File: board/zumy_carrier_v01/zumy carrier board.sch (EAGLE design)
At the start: 20 parts, among them IC1 SN74AUP2G17, IC2 SN74AUP2G17, J1 ODROID_POWER, J2 BATT_POWER, M1 POLOLU_STEP_DOWN, M2 ITG/MPU_MODULE, M3 POLOLU_DRV8833_MODULE, SW1 500SSP1S1M6QEA

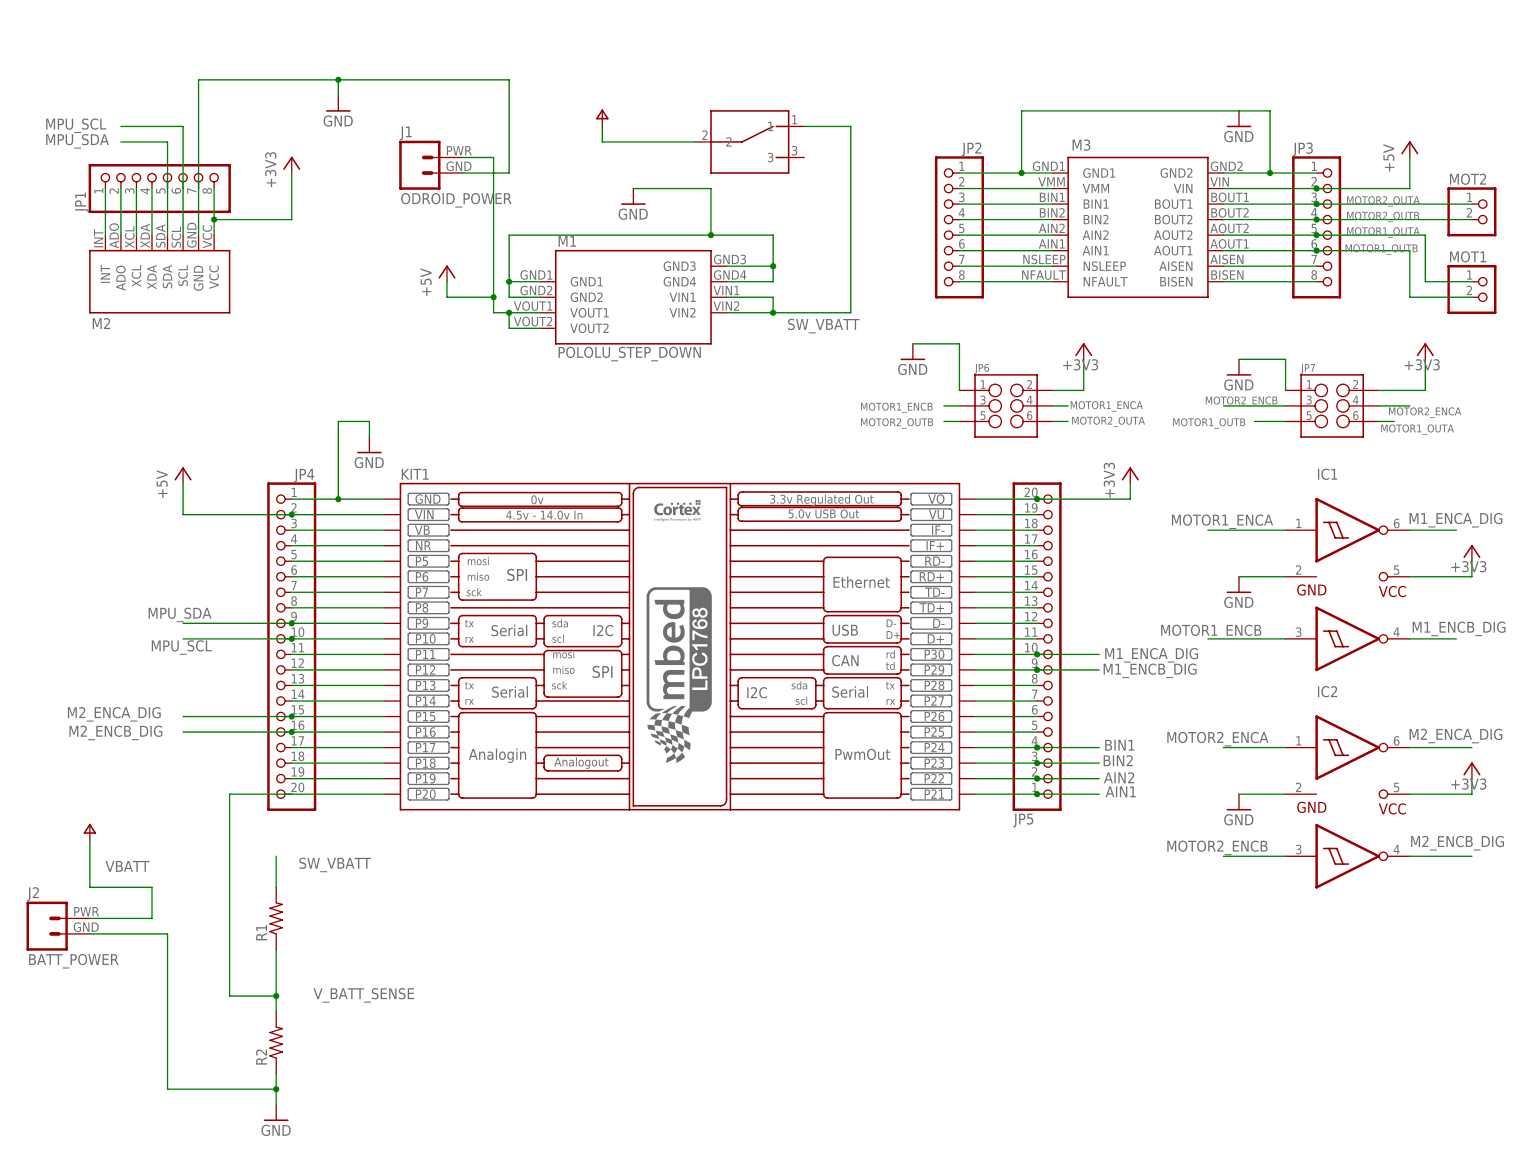
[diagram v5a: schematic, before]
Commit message: Added Rev. E Parts (5V Reg with UVLO, Cap on vsense, caps on level translators). Before ripup and rearrange.
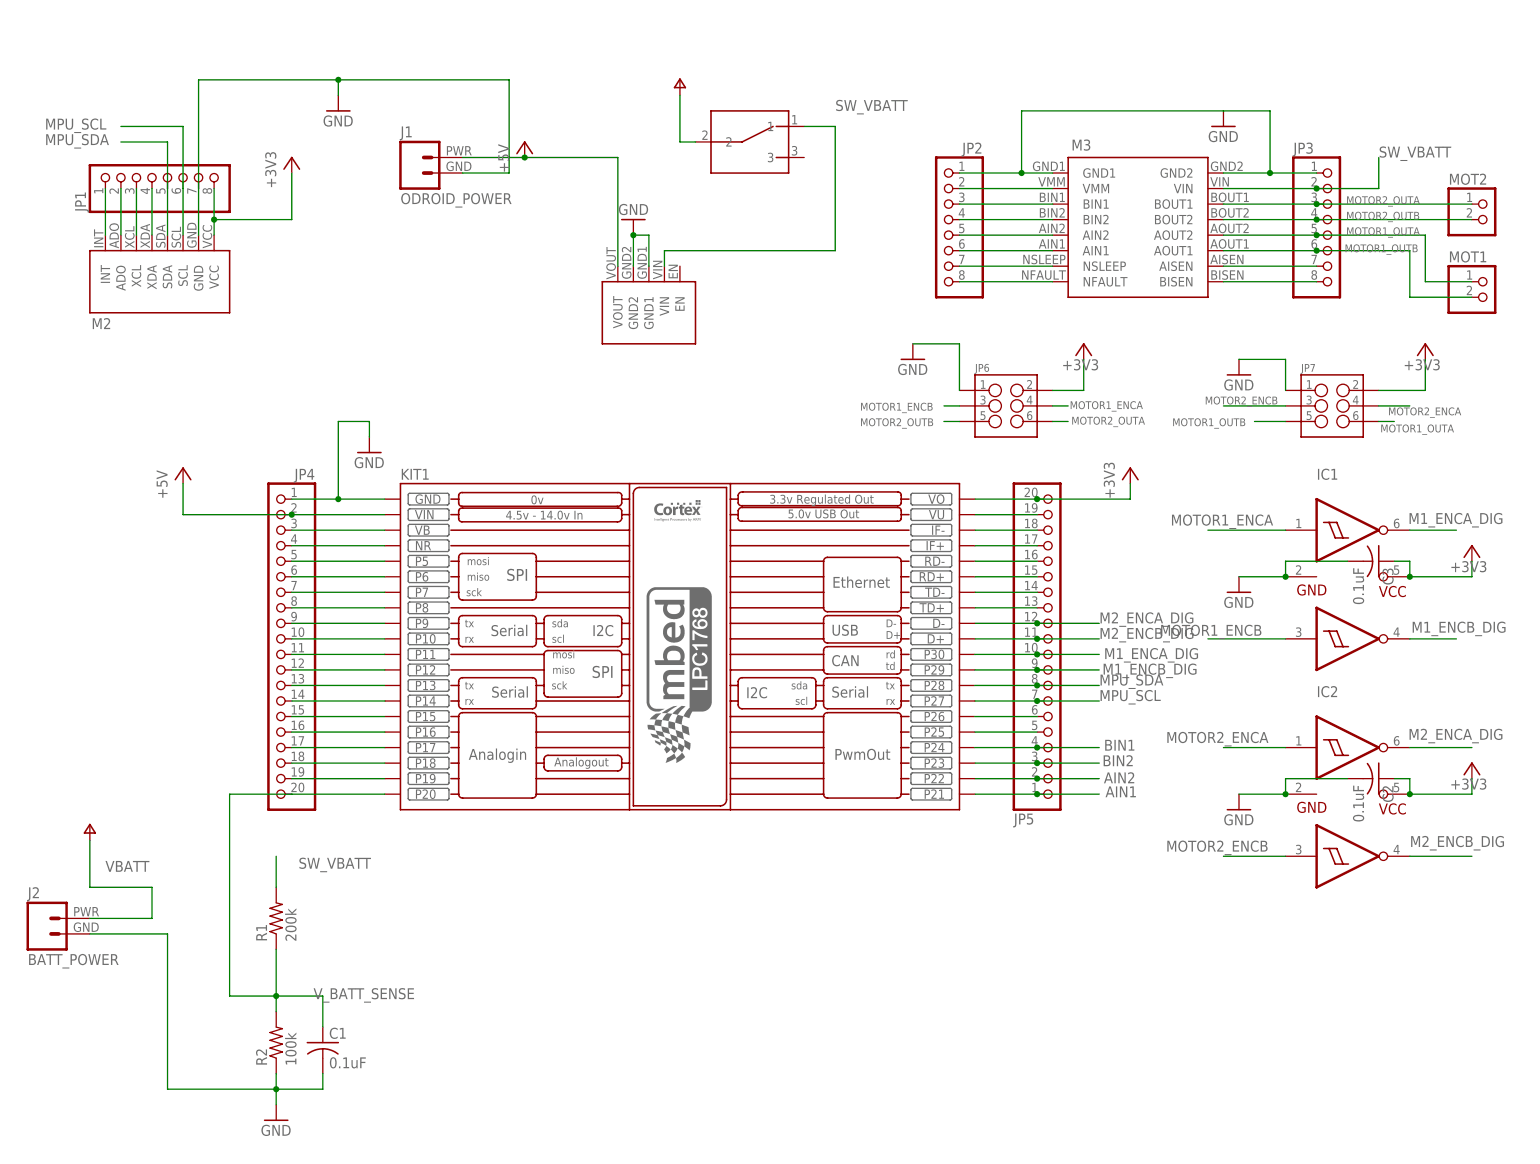
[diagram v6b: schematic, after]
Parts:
- removed M1: POLOLU_STEP_DOWN, zumy:POLOLU_STEP_DOWN
- added C1, C2, C3: 0.1uF, rcl:C-USC1206
- added U$5: POLOLU_D24V50F5, zumy:POLOLU_D24V50F5
- R1: value (none) -> 200k; device resistor:R-US_0204/5 -> resistor:R-US_R1206
- R2: value (none) -> 100k; device resistor:R-US_0204/5 -> resistor:R-US_R1206
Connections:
- removed net N$35: JP5.7, KIT1.P27
- removed net N$36: JP5.8, KIT1.P28
- removed net N$39: JP5.11, KIT1.D+
- removed net N$40: JP5.12, KIT1.D-
- new net N$10: JP4.16, KIT1.P16
- new net N$7: JP4.9, KIT1.P9
- new net N$8: JP4.10, KIT1.P10
- new net N$9: JP4.15, KIT1.P15
- net +3V3: now also C2.1, C3.1
- net +5V: now also U$5.VOUT; no longer JP3.2, M1.VOUT1, M1.VOUT2, M3.VIN
- net GND: now also C1.2, C2.2, C3.2, U$5.GND1, U$5.GND2; no longer M1.GND1, M1.GND2, M1.GND3, M1.GND4
- net M2_ENCA_DIG: now also JP5.12, KIT1.D-; no longer JP4.15, KIT1.P15
- net M2_ENCB_DIG: now also JP5.11, KIT1.D+; no longer JP4.16, KIT1.P16
- net MPU_SCL: now also JP5.7, KIT1.P27; no longer JP4.10, KIT1.P10
- net MPU_SDA: now also JP5.8, KIT1.P28; no longer JP4.9, KIT1.P9
- net SW_VBATT: now also JP3.2, M3.VIN, U$5.VIN; no longer M1.VIN1, M1.VIN2
- net V_BATT_SENSE: now also C1.1

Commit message: Schematic and part placement mostly done. Need to clean up schematic, then fine adjust layout, then ready for routing.
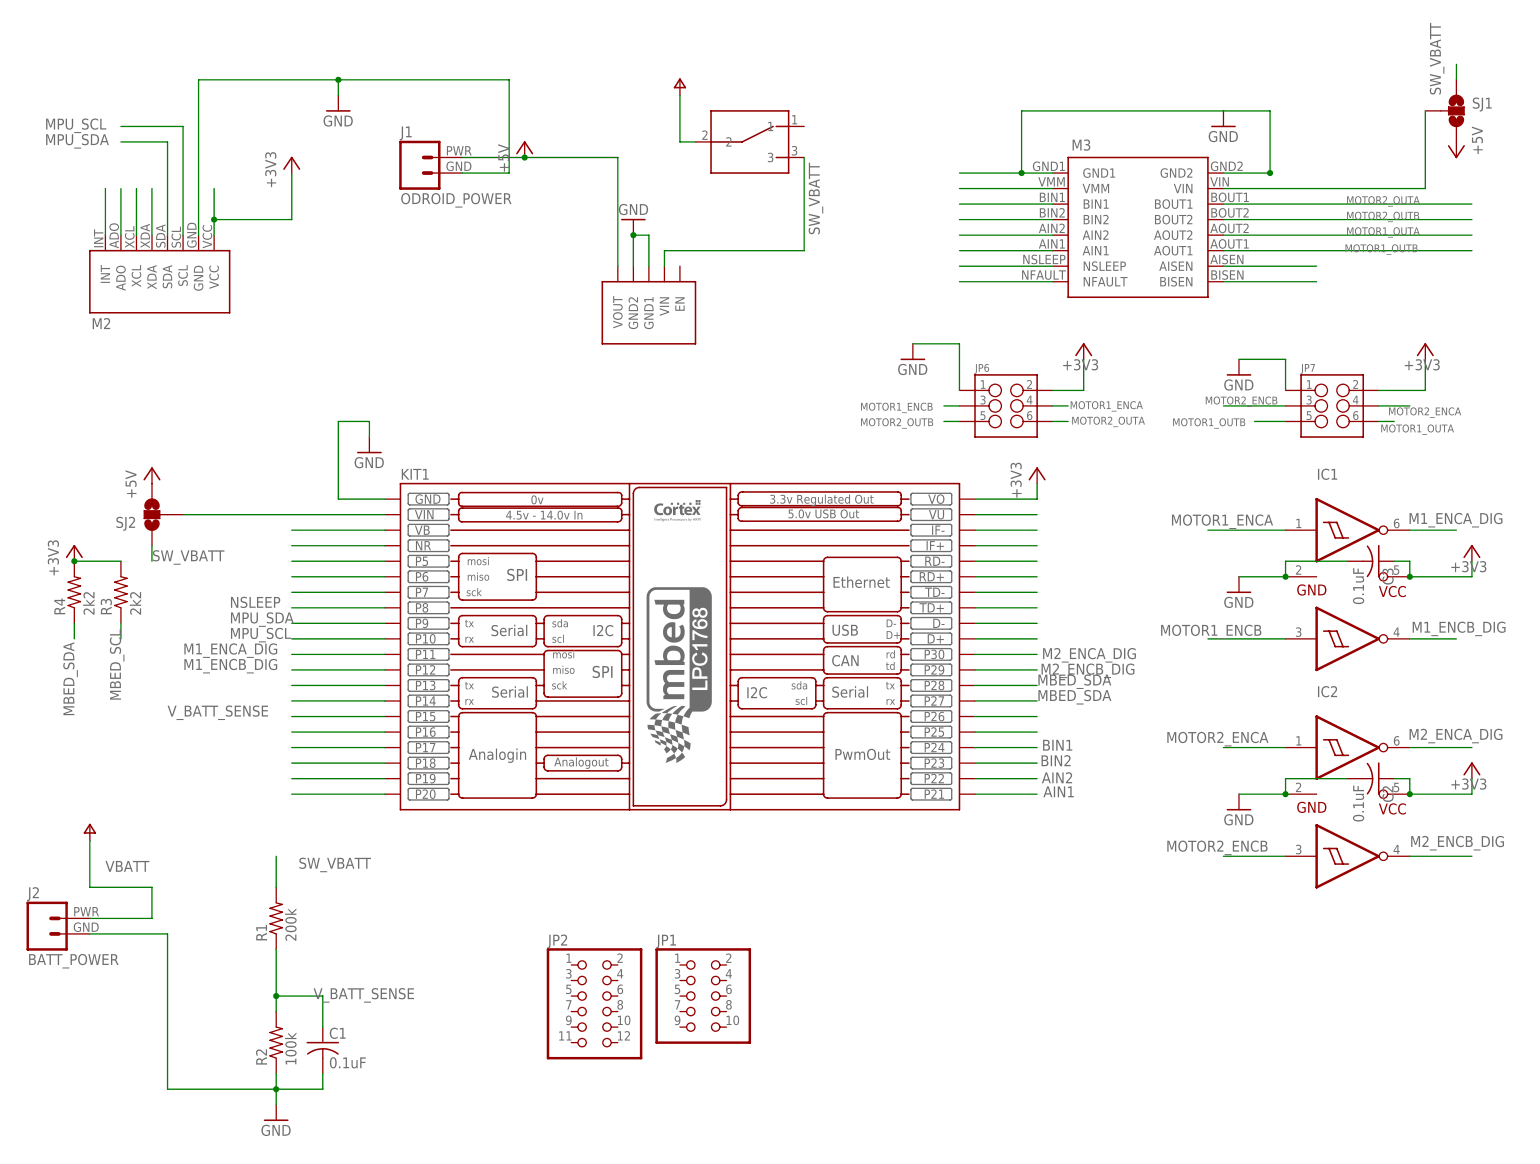
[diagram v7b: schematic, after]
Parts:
- removed JP3: (no value), zumy:PINHD-1X8
- removed JP4, JP5: (no value), zumy:PINHD-1X20
- removed MOT1, MOT2: (no value), pinhead:PINHD-1X2
- added R3, R4: 2k2, resistor:R-US_R1206
- added SJ1, SJ2: (no value), SparkFun-Passives:SOLDERJUMPER_2WAYT
- JP1: device zumy:PINHD-1X8 -> pinhead:PINHD-2X5
- JP2: device zumy:PINHD-1X8 -> pinhead:PINHD-2X6
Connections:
- removed net N$19: JP4.11, KIT1.P11
- removed net N$20: JP4.12, KIT1.P12
- removed net N$55: JP2.7, M3.NSLEEP
- removed net N$8: JP4.10, KIT1.P10
- removed net N$9: JP4.15, KIT1.P15
- new net MBED_SCL: KIT1.P27, R3.1
- new net MBED_SDA: KIT1.P28, R4.1
- new net N$17: KIT1.VIN, SJ2.2
- new net N$5: KIT1.D-
- new net N$6: KIT1.D+
- new net NSLEEP: KIT1.P8, M3.NSLEEP
- net +3V3: now also R3.2, R4.2; no longer JP1.8, JP5.20
- net +5V: now also SJ1.3, SJ2.3; no longer JP4.2, KIT1.VIN
- net AIN1: no longer JP2.6, JP5.1
- net AIN2: no longer JP2.5, JP5.2
- net BIN1: no longer JP2.3, JP5.4
- net BIN2: no longer JP2.4, JP5.3
- net GND: no longer JP1.7, JP2.1, JP3.1, JP4.1
- net M1_ENCA_DIG: now also KIT1.P11; no longer JP5.10, KIT1.P30
- net M1_ENCB_DIG: now also KIT1.P12; no longer JP5.9, KIT1.P29
- net M2_ENCA_DIG: now also KIT1.P30; no longer JP5.12, KIT1.D-
- net M2_ENCB_DIG: now also KIT1.P29; no longer JP5.11, KIT1.D+
- net MOTOR1_OUTA: no longer JP3.5, MOT1.1
- net MOTOR1_OUTB: no longer JP3.6, MOT1.2
- net MOTOR2_OUTA: no longer JP3.3, MOT2.1
- net MOTOR2_OUTB: no longer JP3.4, MOT2.2
- net MPU_SCL: now also KIT1.P10; no longer JP1.6, JP5.7, KIT1.P27
- net MPU_SDA: now also KIT1.P9; no longer JP1.5, JP5.8, KIT1.P28
- net N$1: no longer JP1.1
- net N$10: no longer JP4.16
- net N$11: no longer JP4.3
- net N$12: no longer JP4.4
- net N$13: no longer JP4.5
- net N$14: no longer JP4.6
- net N$15: no longer JP4.7
- net N$16: now also M3.VIN, SJ1.2; no longer JP4.8, KIT1.P8
- net N$2: no longer JP1.2
- net N$21: no longer JP4.13
- net N$22: no longer JP4.14
- net N$25: no longer JP4.17
- net N$26: no longer JP4.18
- net N$27: no longer JP4.19
- net N$3: no longer JP1.3
- net N$33: no longer JP5.5
- net N$34: no longer JP5.6
- net N$4: no longer JP1.4
- net N$41: no longer JP5.13
- net N$42: no longer JP5.14
- net N$43: no longer JP5.15
- net N$44: no longer JP5.16
- net N$45: no longer JP5.17
- net N$46: no longer JP5.18
- net N$47: no longer JP5.19
- net N$50: no longer JP2.2
- net N$56: no longer JP2.8
- net N$63: no longer JP3.7
- net N$64: no longer JP3.8
- net N$7: now also KIT1.P20; no longer JP4.9, KIT1.P9
- net SW_VBATT: now also SJ1.1, SJ2.1, SW1.3; no longer JP3.2, M3.VIN, SW1.1
- net V_BATT_SENSE: now also KIT1.P15; no longer JP4.20, KIT1.P20

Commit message: First pass at layout done
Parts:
- removed JP6, JP7: (no value), SparkFun-Connectors:M03X2SHROUD
- removed M3: POLOLU_DRV8833_MODULE, zumy:POLOLU_DRV8833_MODULE
- added M1: (no value), SparkFun-Connectors:M03X2SHROUD
- added MOT_DRIVE: POLOLU_DRV8833_MODULE, zumy:POLOLU_DRV8833_MODULE
- added MPU: ITG/MPU_MODULE, zumy:ITG/MPU_MODULE
- M2: value ITG/MPU_MODULE -> (none); device zumy:ITG/MPU_MODULE -> SparkFun-Connectors:M03X2SHROUD
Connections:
- net VBATT renamed N$2
- net V_BATT_SENSE renamed BATT_SENSE
- removed net AIN1: KIT1.P21, M3.AIN1
- removed net AIN2: KIT1.P22, M3.AIN2
- removed net BIN1: KIT1.P24, M3.BIN1
- removed net BIN2: KIT1.P23, M3.BIN2
- removed net M1_ENCA_DIG: IC1.1Y, KIT1.P11
- removed net M1_ENCB_DIG: IC1.2Y, KIT1.P12
- removed net M2_ENCA_DIG: IC2.1Y, KIT1.P30
- removed net M2_ENCB_DIG: IC2.2Y, KIT1.P29
- removed net MOTOR1_ENCA: IC1.1A, JP6.4
- removed net MOTOR1_ENCB: IC1.2A, JP6.3
- removed net MOTOR1_OUTA: JP7.6, M3.AOUT2
- removed net MOTOR1_OUTB: JP7.5, M3.AOUT1
- removed net MOTOR2_ENCA: IC2.1A, JP7.4
- removed net MOTOR2_ENCB: IC2.2A, JP7.3
- removed net MOTOR2_OUTA: JP6.6, M3.BOUT1
- removed net MOTOR2_OUTB: JP6.5, M3.BOUT2
- removed net N$1 (its old number): M2.INT
- removed net N$10: KIT1.P16
- removed net N$11: KIT1.VB
- removed net N$12: KIT1.NR
- removed net N$13: KIT1.P5
- removed net N$14: KIT1.P6
- removed net N$15: KIT1.P7
- removed net N$16: M3.VIN, SJ1.2
- removed net N$2 (its old number): M2.ADO
- removed net N$21: KIT1.P13
- removed net N$22: KIT1.P14
- removed net N$25: KIT1.P17
- removed net N$26: KIT1.P18
- removed net N$27: KIT1.P19
- removed net N$33: KIT1.P25
- removed net N$34: KIT1.P26
- removed net N$4: M2.XDA
- removed net N$41: KIT1.TD+
- removed net N$42: KIT1.TD-
- removed net N$43: KIT1.RD+
- removed net N$44: KIT1.RD-
- removed net N$45: KIT1.IF+
- removed net N$46: KIT1.IF-
- removed net N$47: KIT1.VU
- removed net N$5: KIT1.D-
- removed net N$50: M3.VMM
- removed net N$56: M3.NFAULT
- removed net N$6: KIT1.D+
- removed net N$63: M3.AISEN
- removed net N$64: M3.BISEN
- removed net N$7: KIT1.P20
- removed net NSLEEP: KIT1.P8, M3.NSLEEP
- removed net SW_VBATT: R1.2, SJ1.1, SJ2.1, SW1.3, U$5.VIN
- new net M1_EA: IC1.1A, M1.4
- new net M1_EAD: IC1.1Y, KIT1.P29
- new net M1_EB: IC1.2A, M1.3
- new net M1_EBD: IC1.2Y, KIT1.P30
- new net M1_IN1: KIT1.P21, MOT_DRIVE.AIN1
- new net M1_IN2: KIT1.P22, MOT_DRIVE.AIN2
- new net M1_OUT1: M1.6, MOT_DRIVE.AOUT1
- new net M1_OUT2: M1.5, MOT_DRIVE.AOUT2
- new net M2_EA: IC2.1A, M2.4
- new net M2_EAD: IC2.1Y, KIT1.P11
- new net M2_EB: IC2.2A, M2.3
- new net M2_EBD: IC2.2Y, KIT1.P12
- new net M2_IN1: KIT1.P24, MOT_DRIVE.BIN1
- new net M2_IN2: KIT1.P23, MOT_DRIVE.BIN2
- new net M2_OUT1: M2.6, MOT_DRIVE.BOUT1
- new net M2_OUT2: M2.5, MOT_DRIVE.BOUT2
- new net MBED_A0: JP2.12, KIT1.P16
- new net MBED_A1: JP2.10, KIT1.P17
- new net MBED_A2: JP2.8, KIT1.P18
- new net MBED_A3: JP2.6, KIT1.P19
- new net MBED_MISO: JP2.9, KIT1.P6
- new net MBED_MOSI: JP2.11, KIT1.P5
- new net MBED_PWM0: JP1.6, KIT1.P25
- new net MBED_PWM1: JP1.5, KIT1.P26
- new net MBED_RX: JP1.4, KIT1.P14
- new net MBED_SCK: JP2.7, KIT1.P7
- new net MBED_SS: JP2.5, KIT1.P20
- new net MBED_TX: JP1.2, KIT1.P13
- new net M_SLEEP: KIT1.P8, MOT_DRIVE.NSLEEP
- new net V+: JP2.4, R1.2, SJ1.1, SJ2.3, SW1.3, U$5.VIN
- net +3V3: now also JP2.3, M1.2, M2.2, MPU.VCC; no longer JP6.2, JP7.2, M2.VCC
- net +5V: now also JP1.7, JP1.8, JP2.2, SJ2.1; no longer SJ2.3
- net GND: now also JP1.10, JP1.9, JP2.1, M1.1, M2.1, MOT_DRIVE.GND1, MOT_DRIVE.GND2, MPU.GND; no longer JP6.1, JP7.1, M2.GND, M3.GND1, M3.GND2
- net MBED_SCL: now also JP1.3
- net MBED_SDA: now also JP1.1
- net MPU_SCL: now also MPU.SCL; no longer M2.SCL
- net MPU_SDA: now also MPU.SDA; no longer M2.SDA
- net N$3: now also MOT_DRIVE.VIN, SJ1.2; no longer M2.XCL
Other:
- note added: "Battery Sense"
- note added: "Headers"
- note added: "I2C"
- note added: "MPU"
- note added: "Motors"
- note added: "Power"
- note added: "mbed"
- moved on the sheet: C1, C2, C3, IC1, IC2, J1, J2, JP1, JP2, KIT1, R1, R2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
